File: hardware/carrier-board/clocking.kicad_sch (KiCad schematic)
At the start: 1 part, among them U1 Si5341A-B-GM

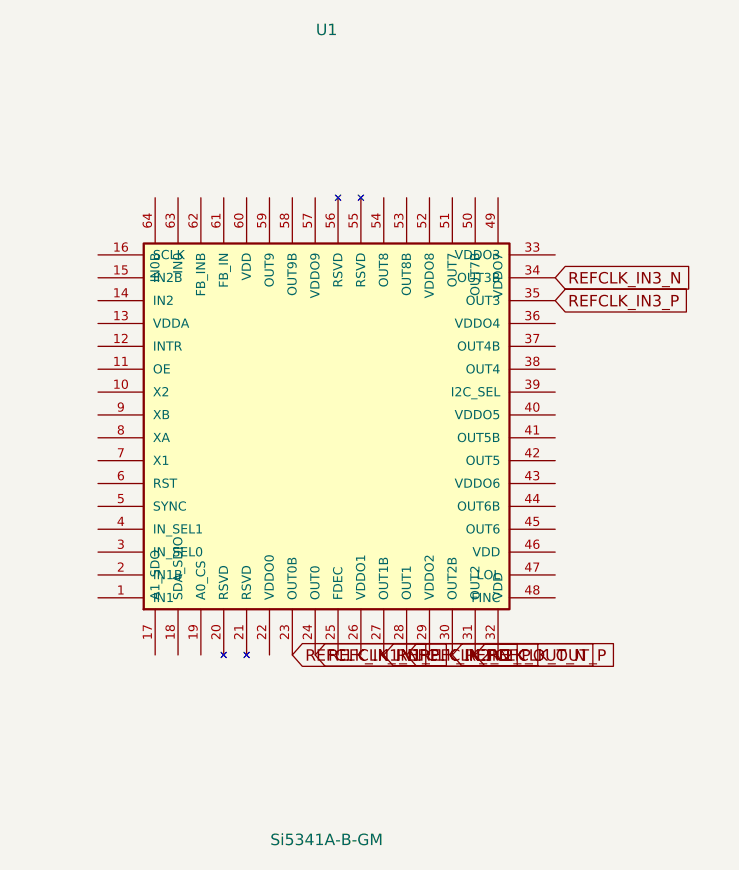
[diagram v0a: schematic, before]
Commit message: Add decoupling capacitors to TXS0102 and Si5341A via Konnect MCP
Switches this project's KiCad schematic editing from hand-authored
S-expression scripts to Konnect's MCP tools, per the konnect skill's
operating rules -- a safer, validated API for schematic edits.

Ran Konnect's design_review/audit_decoupling for the first time on
this project and found a real, previously-missed gap: no decoupling
capacitors existed anywhere in the design. Adds 100nF caps for
TXS0102's VCCA/VCCB (all 4 HDMI sheets) and all 14 of Si5341A's
VDD-family pins (VDDA, VDD x3, VDDO0-9). These still show
power_pin_not_driven in ERC, correctly -- a capacitor doesn't power a
chip, and no regulator feeds these rails yet, which is the separate,
already-documented VCCO regulator open item.

Documents several real Konnect tool quirks discovered along the way:
connect_pins between exactly-coincident pins writes a zero-length
wire that doesn't register in net tracing; move_schematic_component
doesn't adjust connected wires; delete_schematic_net_label matches by
coordinate only and can delete an unrelated pre-existing label (this
happened to two legitimate Task-32 +3V3 labels, caught and restored);
batch_connect_to_net always creates local not global labels; and one
sequence of failed delete calls corrupted clocking.kicad_sch outright,
recovered via git checkout since nothing had been committed yet.
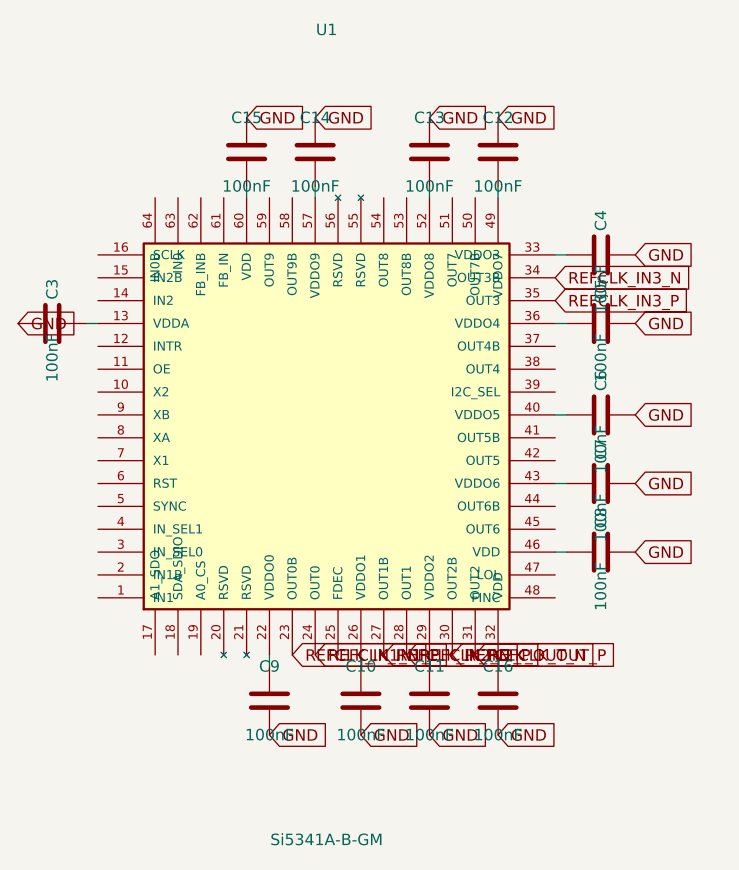
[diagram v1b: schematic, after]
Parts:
- added C10, C11, C12, C13, C14, C15, C16, C3, C4, C5, C6, C7, C8, C9: 100nF, symbol Device:C
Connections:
- net at U1.13 (VDDA): now also C3.2
- net at U1.22 (VDDO0): now also C9.1
- net at U1.26 (VDDO1): now also C10.1
- net at U1.29 (VDDO2): now also C11.1
- net at U1.32 (VDD): now also C16.1
- net at U1.33 (VDDO3): now also C4.1
- net at U1.36 (VDDO4): now also C5.1
- net at U1.40 (VDDO5): now also C6.1
- net at U1.43 (VDDO6): now also C7.1
- net at U1.46 (VDD): now also C8.1
- net at U1.49 (VDDO7): now also C12.2
- net at U1.52 (VDDO8): now also C13.2
- net at U1.57 (VDDO9): now also C14.2
- net at U1.60 (VDD): now also C15.2
- new net GND: C10.2, C11.2, C12.1, C13.1, C14.1, C15.1, C16.2, C3.1, C4.2, C5.2, C6.2, C7.2, C8.2, C9.2

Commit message: Assign footprints to all new decoupling capacitors
Konnect's check_bom_health audit caught a real gap the ERC-based
workflow wouldn't have: add_schematic_component has no footprint
parameter, so all 22 new 100nF decoupling caps (C1/C2 in each HDMI
sheet, C3-C16 in clocking.kicad_sch) were missing one entirely --
would have blocked PCB layout. Assigned the standard
Capacitor_SMD:C_0402_1005Metric footprint to each.
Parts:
- C10, C11, C12, C13, C14, C15, C16, C3, C4, C5, C6, C7, C8, C9: footprint (none) -> Capacitor_SMD:C_0402_1005Metric
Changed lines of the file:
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@@
 			)
 		)
-		(property "Footprint" ""
+		(property "Footprint" "Capacitor_SMD:C_0402_1005Metric"
 			(at 118.11 129.54 0)
 			(hide yes)
@@
 			)
 		)
-		(property "Footprint" ""
+		(property "Footprint" "Capacitor_SMD:C_0402_1005Metric"
 			(at 129.54 97.79 0)
 			(hide yes)
@@
 			)
 		)
-		(property "Footprint" ""
+		(property "Footprint" "Capacitor_SMD:C_0402_1005Metric"
 			(at 129.54 80.01 0)
 			(hide yes)
@@
 			)
 		)
-		(property "Footprint" ""
+		(property "Footprint" "Capacitor_SMD:C_0402_1005Metric"
 			(at 110.49 129.54 0)
 			(hide yes)
@@
 			)
 		)
-		(property "Footprint" ""
+		(property "Footprint" "Capacitor_SMD:C_0402_1005Metric"
 			(at 129.54 113.03 0)
 			(hide yes)
@@
 			)
 		)
-		(property "Footprint" ""
+		(property "Footprint" "Capacitor_SMD:C_0402_1005Metric"
 			(at 110.49 68.58 0)
 			(hide yes)
@@
 			)
 		)
-		(property "Footprint" ""
+		(property "Footprint" "Capacitor_SMD:C_0402_1005Metric"
 			(at 102.87 129.54 0)
 			(hide yes)
@@
 			)
 		)
-		(property "Footprint" ""
+		(property "Footprint" "Capacitor_SMD:C_0402_1005Metric"
 			(at 97.79 68.58 0)
 			(hide yes)
@@
 			)
 		)
-		(property "Footprint" ""
+		(property "Footprint" "Capacitor_SMD:C_0402_1005Metric"
 			(at 92.71 129.54 0)
 			(hide yes)
@@
 			)
 		)
-		(property "Footprint" ""
+		(property "Footprint" "Capacitor_SMD:C_0402_1005Metric"
 			(at 68.58 87.63 0)
 			(hide yes)
@@
 			)
 		)
-		(property "Footprint" ""
+		(property "Footprint" "Capacitor_SMD:C_0402_1005Metric"
 			(at 129.54 105.41 0)
 			(hide yes)
@@
 			)
 		)
-		(property "Footprint" ""
+		(property "Footprint" "Capacitor_SMD:C_0402_1005Metric"
 			(at 129.54 87.63 0)
 			(hide yes)
@@
 			)
 		)
-		(property "Footprint" ""
+		(property "Footprint" "Capacitor_SMD:C_0402_1005Metric"
 			(at 118.11 68.58 0)
 			(hide yes)
@@
 			)
 		)
-		(property "Footprint" ""
+		(property "Footprint" "Capacitor_SMD:C_0402_1005Metric"
 			(at 90.17 68.58 0)
 			(hide yes)
